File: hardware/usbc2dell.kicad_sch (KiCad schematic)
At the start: 23 parts, among them J1 TYPE-C-31-M-17, J2 WJ15EDGRC-3.81-3P, Q1 DOD50P06, Q2 MMBT5551, SW1 DSWB04LHGET, U1 ATtiny1616-M, U2 FUSB302BMPX, U3 L7805, U4 SRV05-4

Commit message: nicer traces + mosfet still fucked
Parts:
- Q1: value DOD50P06 -> (none); symbol Transistor_FET:Q_PMOS_GDS -> Transistor_FET:Q_PMOS_GSD; LCSC C41430590 -> (none)
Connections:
- net VBUS: now also Q1.2 (S); no longer Q1.3 (S)
- net Vout: now also Q1.3 (D); no longer Q1.2 (D)
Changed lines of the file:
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@@
 	)
 	(symbol
-		(lib_id "Transistor_FET:Q_PMOS_GDS")
+		(lib_id "Transistor_FET:Q_PMOS_GSD")
 		(at 130.81 40.64 270)
 		(mirror x)
@@
 			)
 		)
-		(property "Value" "DOD50P06"
+		(property "Value" ""
 			(at 130.81 34.29 90)
 			(effects
@@
 			)
 		)
-		(property "Description" "P-MOSFET transistor, gate/drain/source"
+		(property "Description" "P-MOSFET transistor, gate/source/drain"
 			(at 130.81 40.64 0)
 			(effects
 				(font
-					(size 1.27 1.27)
-				)
-				(hide yes)
-			)
-		)
-		(property "LCSC" "C41430590"
-			(at 130.81 40.64 90)
-			(effects
-				(font

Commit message: attempt to fix mosfet
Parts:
- Q1: value (none) -> DOD50P06; symbol Transistor_FET:Q_PMOS_GSD -> Transistor_FET:Q_PMOS_GDS; LCSC (none) -> C41430590
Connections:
- net VBUS: now also Q1.3 (S); no longer Q1.2 (S)
- net Vout: now also Q1.2 (D); no longer Q1.3 (D)
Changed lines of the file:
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@@
 	)
 	(symbol
-		(lib_id "Transistor_FET:Q_PMOS_GSD")
+		(lib_id "Transistor_FET:Q_PMOS_GDS")
 		(at 130.81 40.64 270)
 		(mirror x)
@@
 			)
 		)
-		(property "Value" ""
+		(property "Value" "DOD50P06"
 			(at 130.81 34.29 90)
 			(effects
@@
 			)
 		)
-		(property "Description" "P-MOSFET transistor, gate/source/drain"
+		(property "Description" "P-MOSFET transistor, gate/drain/source"
 			(at 130.81 40.64 0)
 			(effects
 				(font
+					(size 1.27 1.27)
+				)
+				(hide yes)
+			)
+		)
+		(property "LCSC" "C41430590"
+			(at 130.81 40.64 90)
+			(effects
+				(font

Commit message: correct 7805 part num
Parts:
- U3: value L7805 -> MC7805CDTRKG
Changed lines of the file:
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@@
 			)
 		)
-		(property "Value" "L7805"
+		(property "Value" "MC7805CDTRKG"
 			(at 99.06 34.29 0)
 			(effects
@@
 			)
 		)
-		(property "Datasheet" "http://www.st.com/content/ccc/resource/technical/document/datasheet/41/4f/b3/b0/12/d4/47/88/CD00000444.pdf/files/CD00000444.pdf/jcr:content/translations/en.CD00000444.pdf"
+		(property "Datasheet" "https://www.lcsc.com/datasheet/lcsc_datasheet_2410121902_onsemi-MC7805CDTRKG_C54285.pdf"
 			(at 99.06 39.37 0)
 			(effects

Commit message: comp sel
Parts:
- U3: value MC7805CDTRKG -> L78M05ABDT-TR; LCSC C54285 -> C58069
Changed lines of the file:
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@@
 			)
 		)
-		(property "Value" "MC7805CDTRKG"
+		(property "Value" "L78M05ABDT-TR"
 			(at 99.06 34.29 0)
 			(effects
@@
 			)
 		)
-		(property "Datasheet" "https://www.lcsc.com/datasheet/lcsc_datasheet_2410121902_onsemi-MC7805CDTRKG_C54285.pdf"
+		(property "Datasheet" "https://www.lcsc.com/datasheet/lcsc_datasheet_2307281528_STMicroelectronics-L78M05ABDT-TR_C58069.pdf"
 			(at 99.06 39.37 0)
 			(effects
@@
 			)
 		)
-		(property "Description" "Positive 1.5A 35V Linear Regulator, Fixed Output 5V, TO-220/TO-263/TO-252"
+		(property "Description" ""
 			(at 99.06 38.1 0)
 			(effects
@@
 			)
 		)
-		(property "LCSC" " C54285"
+		(property "LCSC" "C58069"
 			(at 99.06 38.1 0)
 			(effects

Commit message: put ID pin on pin with DAC capability for possible analog comms in future
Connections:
- net ID: now also U1.7 (PA6); no longer U1.10 (PB4)
- net LED_G: now also U1.5 (PA4); no longer U1.6 (PA5)
- net LED_R: now also U1.6 (PA5); no longer U1.7 (PA6)
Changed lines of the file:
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@@
-	)
-	(no_connect
-		(at 60.96 48.26)
 	)
 	(no_connect
@@
 	)
 	(no_connect
+		(at 60.96 71.12)
+	)
+	(no_connect
 		(at 60.96 45.72)
 	)
@@
 	(wire
 		(pts
+			(xy 60.96 55.88) (xy 69.85 55.88)
+		)
+		(stroke
+			(width 0)
+			(type default)
+		)
+	)
+	(wire
+		(pts
 			(xy 66.04 106.68) (xy 66.04 110.49)
 		)
@@
 	(wire
 		(pts
+			(xy 60.96 53.34) (xy 72.39 53.34)
+		)
+		(stroke
+			(width 0)
+			(type default)
+		)
+	)
+	(wire
+		(pts
 			(xy 31.75 119.38) (xy 31.75 124.46)
 		)
@@
 	(wire
 		(pts
+			(xy 60.96 50.8) (xy 69.85 50.8)
+		)
+		(stroke
+			(width 0)
+			(type default)
+		)
+	)
+	(wire
+		(pts
 			(xy 114.3 55.88) (xy 121.92 55.88)
 		)
@@
 	(wire
 		(pts
-			(xy 60.96 53.34) (xy 69.85 53.34)
-		)
-		(stroke
-			(width 0)
-			(type default)
-		)
-	)
-	(wire
-		(pts
 			(xy 68.58 125.73) (xy 71.12 125.73)
 		)
@@
 	(wire
 		(pts
-			(xy 60.96 55.88) (xy 69.85 55.88)
-		)
-		(stroke
-			(width 0)
-			(type default)
-		)
-	)
-	(wire
-		(pts
 			(xy 69.85 40.64) (xy 60.96 40.64)
 		)
@@
 	(wire
 		(pts
-			(xy 60.96 50.8) (xy 69.85 50.8)
-		)
-		(stroke
-			(width 0)
-			(type default)
-		)
-	)
-	(wire
-		(pts
 			(xy 114.3 38.1) (xy 114.3 55.88)
 		)
@@
 	(wire
 		(pts
-			(xy 60.96 71.12) (xy 72.39 71.12)
-		)
-		(stroke
-			(width 0)
-			(type default)
-		)
-	)
-	(wire
-		(pts
 			(xy 71.12 106.68) (xy 71.12 110.49)
 		)
@@
 		(pts
 			(xy 26.67 68.58) (xy 30.48 68.58)
+		)
+		(stroke
+			(width 0)
+			(type default)
+		)
+	)
+	(wire
+		(pts
+			(xy 60.96 48.26) (xy 69.85 48.26)
 		)
 		(stroke
@@
 		)
 	)
-	(label "LED_G"
-		(at 69.85 50.8 180)
-		(effects
-			(font
-				(size 1.27 1.27)
-			)
-			(justify right bottom)
-		)
-	)
 	(label "ID"
 		(at 144.78 118.11 0)
@@
 		)
 	)
-	(label "ID"
-		(at 72.39 71.12 180)
+	(label "LED_G"
+		(at 69.85 48.26 180)
 		(effects
 			(font
@@
 		)
 	)
-	(label "LED_R"
-		(at 69.85 53.34 180)
-		(effects
-			(font
-				(size 1.27 1.27)
-			)
-			(justify right bottom)
-		)
-	)
 	(label "S2"
 		(at 26.67 66.04 0)
@@
 		)
 	)
+	(label "LED_R"
+		(at 69.85 50.8 180)
+		(effects
+			(font
+				(size 1.27 1.27)
+			)
+			(justify right bottom)
+		)
+	)
 	(label "CC1"
 		(at 181.61 118.11 180)
@@
 		)
 	)
+	(label "ID_PIN"
+		(at 139.7 138.43 90)
+		(effects
+			(font
+				(size 1.27 1.27)
+			)
+			(justify left bottom)
+		)
+	)
+	(label "SDA"
+		(at 77.47 66.04 0)
+		(effects
+			(font
+				(size 1.27 1.27)
+			)
+			(justify left bottom)
+		)
+	)
+	(label "PWR_EN"
+		(at 104.14 128.27 0)
+		(effects
+			(font
+				(size 1.27 1.27)
+			)
+			(justify left bottom)
+		)
+	)
+	(label "LED_B"
+		(at 58.42 124.46 180)
+		(effects
+			(font
+				(size 1.27 1.27)
+			)
+			(justify right bottom)
+		)
+	)
+	(label "PWR_EN"
+		(at 72.39 68.58 180)
+		(effects
+			(font
+				(size 1.27 1.27)
+			)
+			(justify right bottom)
+		)
+	)
+	(label "CC2"
+		(at 116.84 71.12 0)
+		(effects
+			(font
+				(size 1.27 1.27)
+			)
+			(justify left bottom)
+		)
+	)
 	(label "LED_B"
 		(at 69.85 55.88 180)
@@
 		)
 	)
-	(label "ID_PIN"
-		(at 139.7 138.43 90)
-		(effects
-			(font
-				(size 1.27 1.27)
-			)
-			(justify left bottom)
-		)
-	)
-	(label "SDA"
-		(at 77.47 66.04 0)
-		(effects
-			(font
-				(size 1.27 1.27)
-			)
-			(justify left bottom)
-		)
-	)
-	(label "PWR_EN"
-		(at 104.14 128.27 0)
-		(effects
-			(font
-				(size 1.27 1.27)
-			)
-			(justify left bottom)
-		)
-	)
-	(label "LED_B"
-		(at 58.42 124.46 180)
-		(effects
-			(font
-				(size 1.27 1.27)
-			)
-			(justify right bottom)
-		)
-	)
-	(label "PWR_EN"
-		(at 72.39 68.58 180)
-		(effects
-			(font
-				(size 1.27 1.27)
-			)
-			(justify right bottom)
-		)
-	)
-	(label "CC2"
-		(at 116.84 71.12 0)
-		(effects
-			(font
-				(size 1.27 1.27)
-			)
-			(justify left bottom)
-		)
-	)
+	(label "ID"
+		(at 72.39 53.34 180)
+		(effects
+			(font
+				(size 1.27 1.27)
+			)
+			(justify right bottom)
+		)
+	)

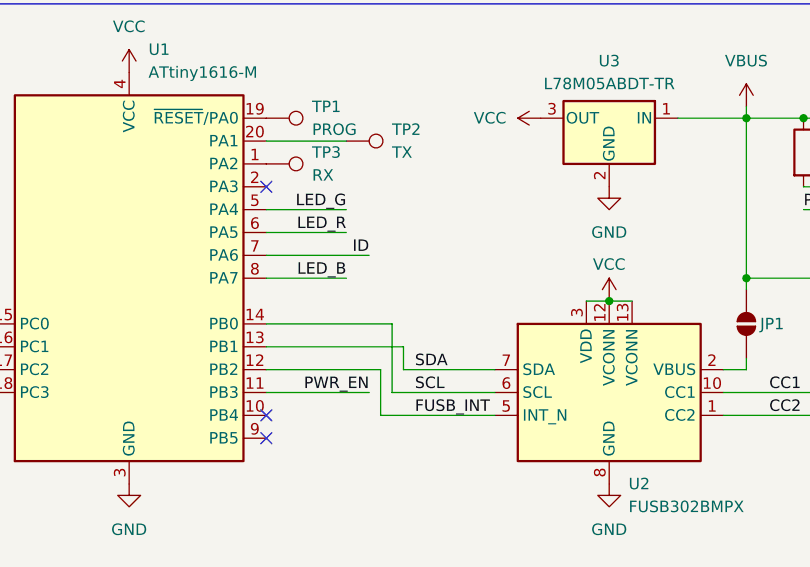
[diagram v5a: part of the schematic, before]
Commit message: [PCB] fix pullups
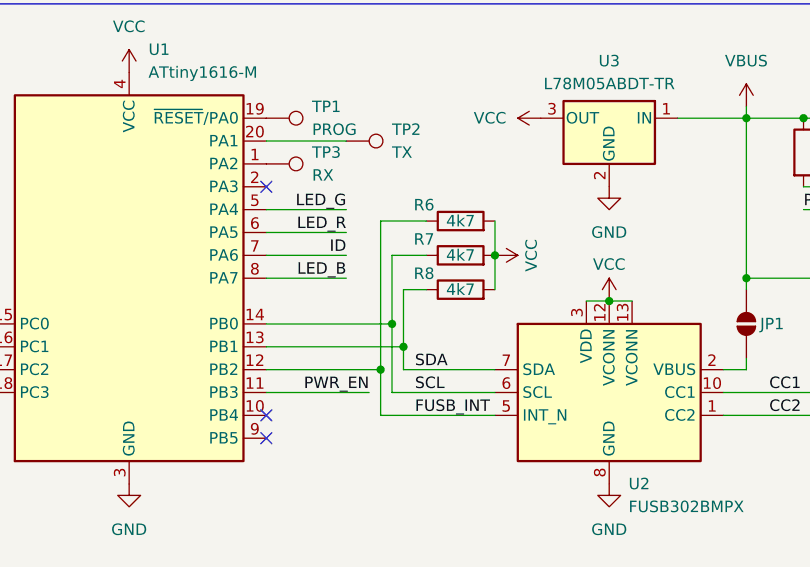
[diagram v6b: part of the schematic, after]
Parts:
- added R6, R7, R8: 4k7, Resistor_SMD:R_0603_1608Metric, symbol Device:R
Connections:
- net FUSB_INT: now also R6.1
- net SCL: now also R7.1
- net SDA: now also R8.1
- net VCC: now also R6.2, R7.2, R8.2
